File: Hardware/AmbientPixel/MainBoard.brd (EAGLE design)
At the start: 65.6 x 56.8 mm, 9 parts

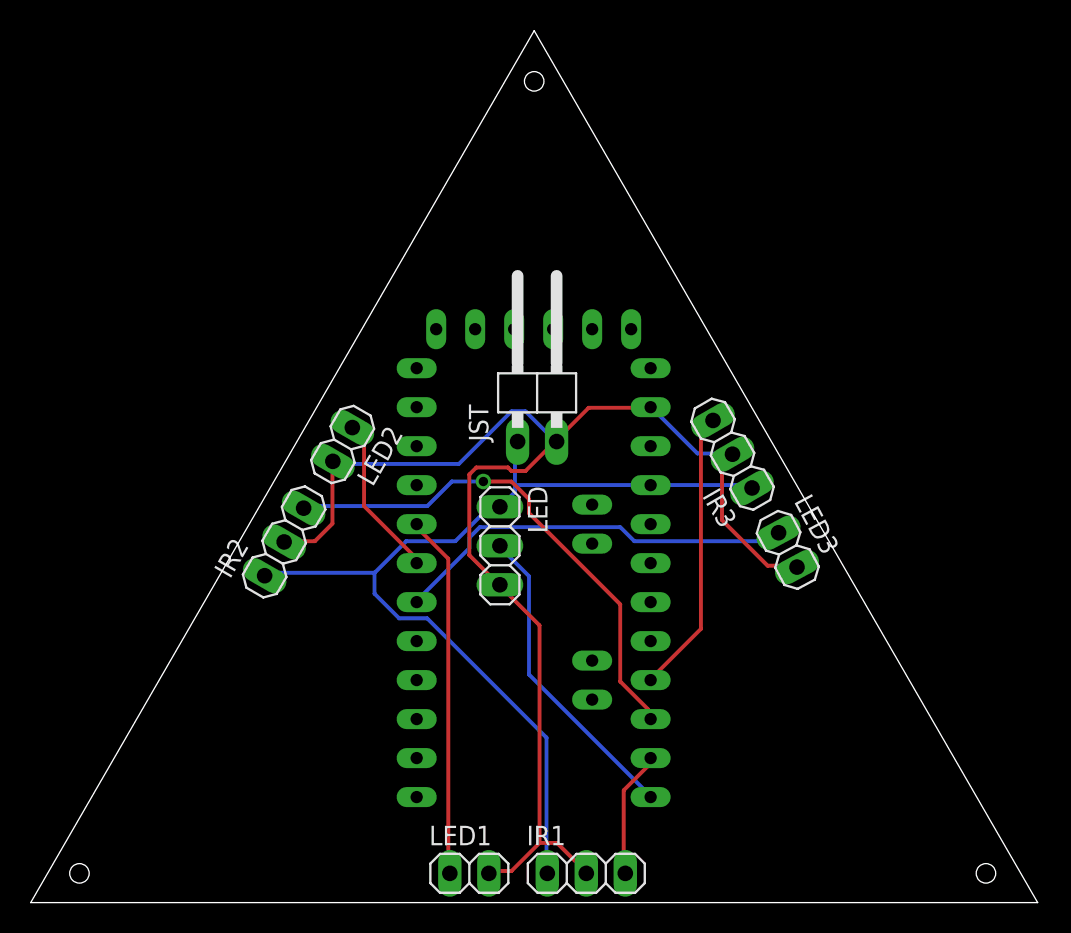
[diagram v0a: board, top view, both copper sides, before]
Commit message: p板に納品したファイルの追加
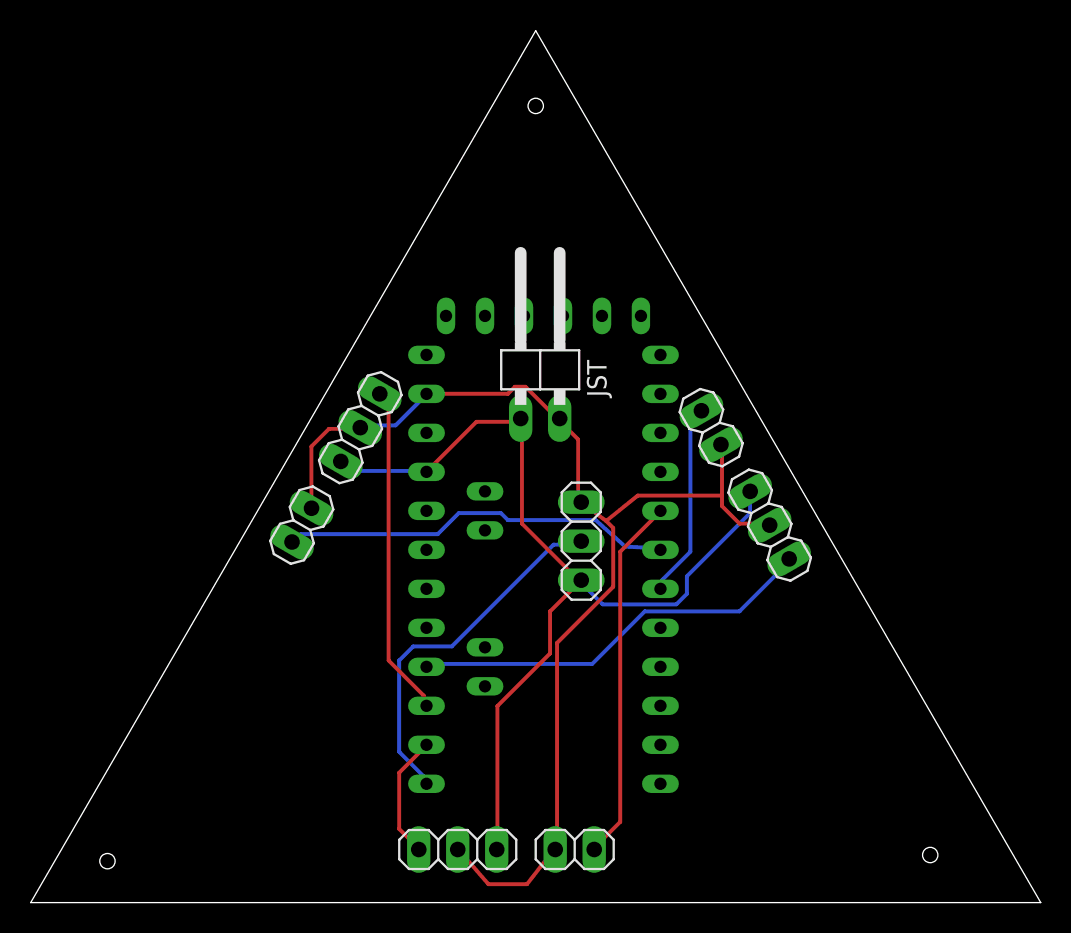
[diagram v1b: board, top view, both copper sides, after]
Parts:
- moved LED3 9.40 mm to (44.3, 30.9), turned to 300 degrees
- moved IR2 8.95 mm to (21.5, 30.9)
- moved IR1 8.52 mm to (27.8, 3.46), turned to 180 degrees
- moved LED1 7.04 mm to (35.4, 3.46), turned to 180 degrees
- moved LED2 5.89 mm to (17.7, 24.6), turned to 60 degrees
- moved LED 5.31 mm to (35.9, 23.5), turned to 90 degrees
- moved IR3 5.22 mm to (48.1, 24.6), turned to 300 degrees
- moved U$1 2.09 mm to (32.1, 23.0), flipped to the bottom
- moved JST 1.51 mm to (33.2, 35.3)
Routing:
- net N$3: track 10.6 -> 25.7 mm
- net N$4: track 26.7 -> 12.7 mm
- net N$6: track 33.5 -> 21.6 mm, vias 1 -> 0
- net GND: track 89.7 -> 78.2 mm
- net N$7: track 18.6 -> 26.7 mm
- net N$1: track 20.4 -> 23.9 mm
- net VDD: track 62.9 -> 61.8 mm
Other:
- board size 65.6 x 56.8 mm -> 65.8 x 56.8 mm
